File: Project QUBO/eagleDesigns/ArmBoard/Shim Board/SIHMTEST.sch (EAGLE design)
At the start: 10 parts, among them U1 BME280

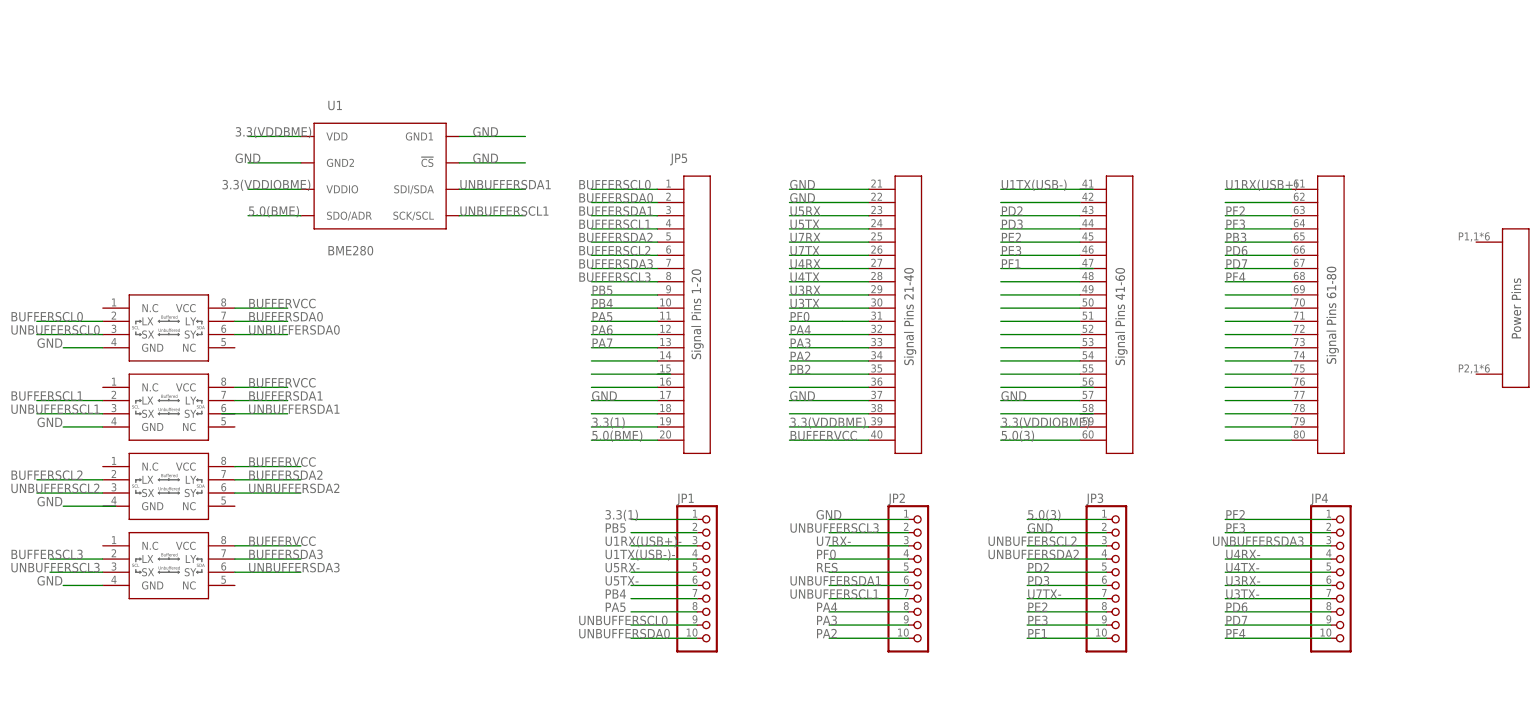
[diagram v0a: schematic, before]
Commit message: 
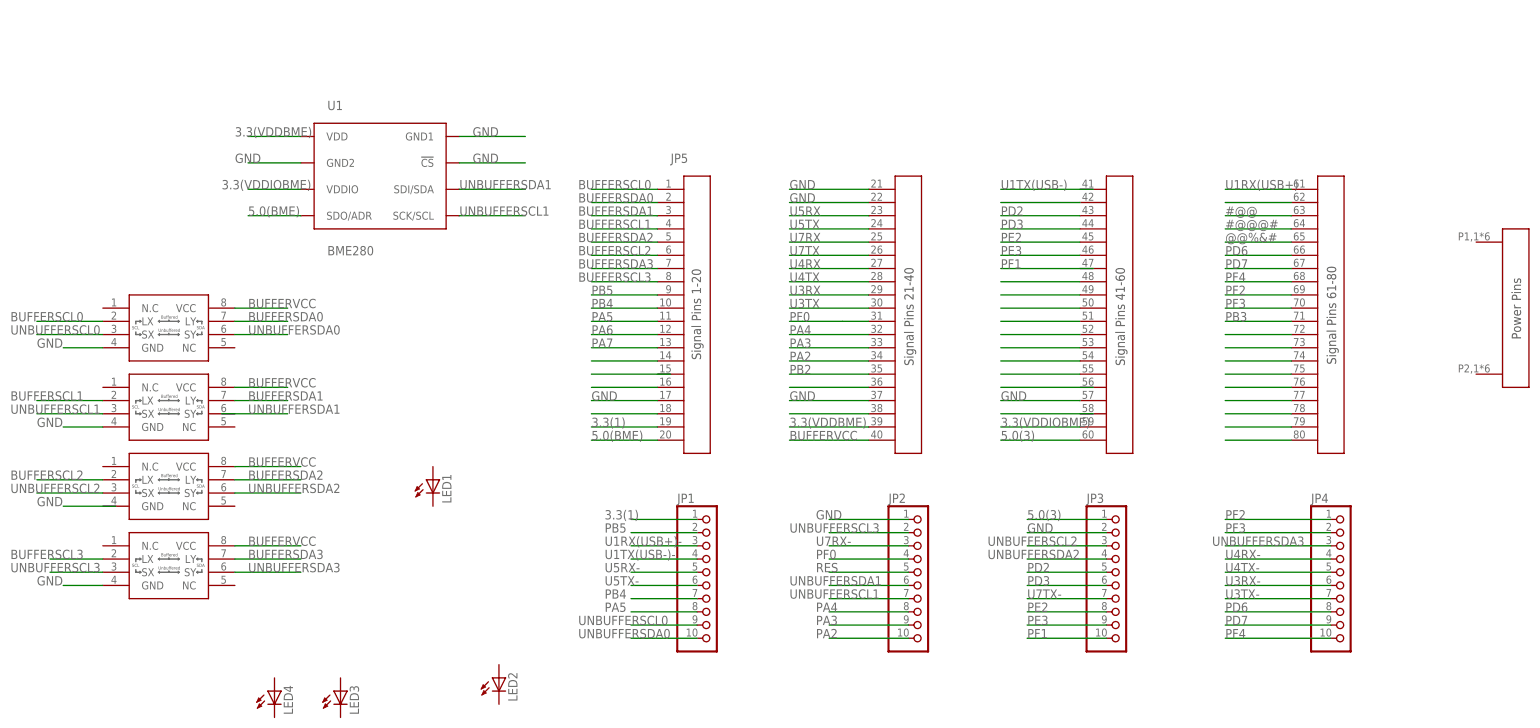
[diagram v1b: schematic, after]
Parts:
- added LED1, LED2, LED3, LED4: (no value), led:LEDCHIPLED_0805
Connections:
- removed net N$38: JP5.P$69
- removed net N$39: JP5.P$70
- removed net N$40: JP5.P$71
- new net #@@: JP5.P$63
- new net #@@@#: JP5.P$64
- new net @@%&#: JP5.P$65
- net PB3: now also JP5.P$71; no longer JP5.P$65
- net PF2: now also JP5.P$69; no longer JP5.P$63
- net PF3: now also JP5.P$70; no longer JP5.P$64

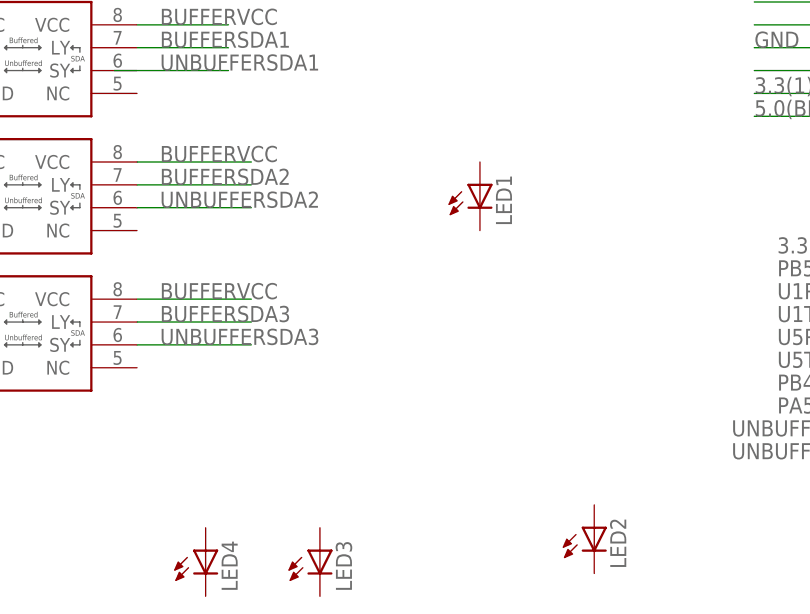
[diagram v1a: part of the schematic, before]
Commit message: 
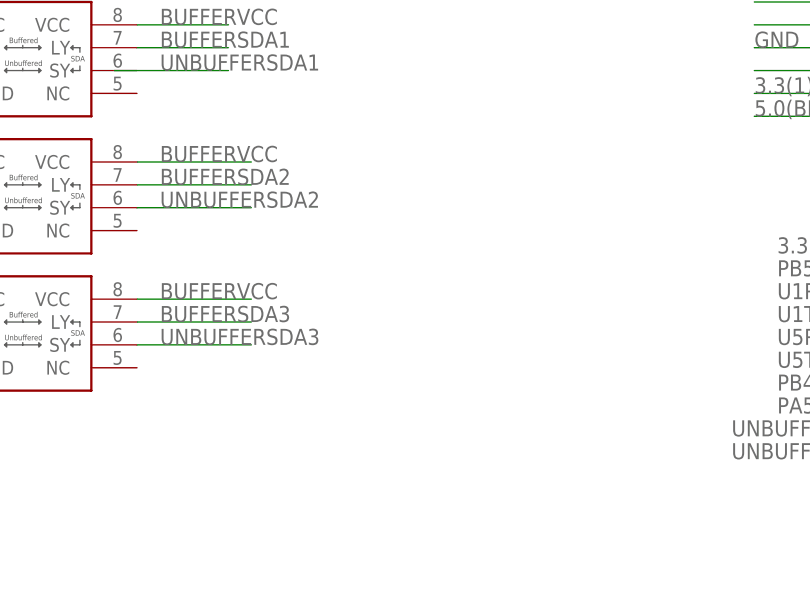
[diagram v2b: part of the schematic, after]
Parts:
- removed LED1, LED2, LED3, LED4: (no value), led:LEDCHIPLED_0805
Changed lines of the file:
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@@
 <part name="U$3" library="NXP" deviceset="P82B715" device=""/>
 <part name="U$4" library="NXP" deviceset="P82B715" device=""/>
-<part name="LED1" library="led" deviceset="LED" device="CHIPLED_0805"/>
-<part name="LED2" library="led" deviceset="LED" device="CHIPLED_0805"/>
-<part name="LED3" library="led" deviceset="LED" device="CHIPLED_0805"/>
-<part name="LED4" library="led" deviceset="LED" device="CHIPLED_0805"/>
 </parts>
 <sheets>
@@
 <instance part="U$3" gate="G$1" x="-86.36" y="93.98"/>
 <instance part="U$4" gate="G$1" x="-86.36" y="78.74"/>
-<instance part="LED1" gate="G$1" x="-35.56" y="96.52"/>
-<instance part="LED2" gate="G$1" x="-22.86" y="58.42"/>
-<instance part="LED3" gate="G$1" x="-53.34" y="55.88"/>
-<instance part="LED4" gate="G$1" x="-66.04" y="55.88"/>
 </instances>
 <busses>

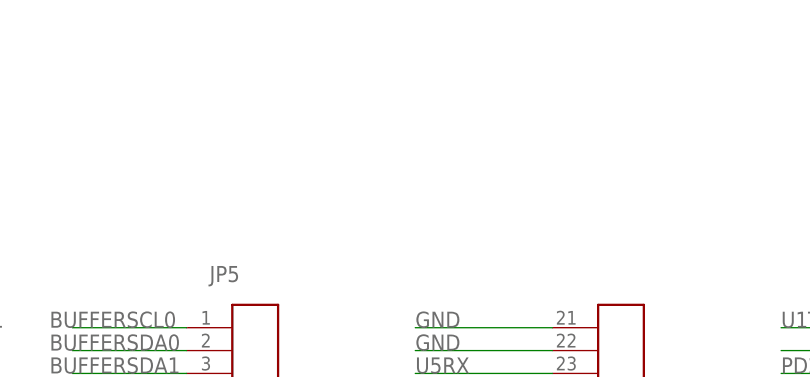
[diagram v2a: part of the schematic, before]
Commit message: 
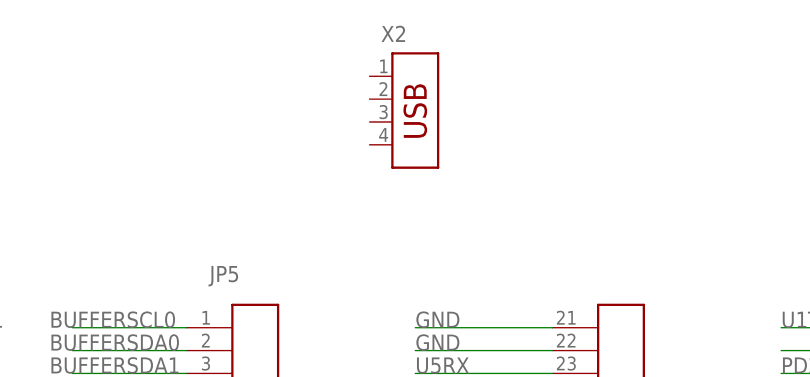
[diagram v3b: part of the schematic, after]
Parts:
- added X2: (no value), con-amp:USB-787616
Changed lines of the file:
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@@
 <part name="U$3" library="NXP" deviceset="P82B715" device=""/>
 <part name="U$4" library="NXP" deviceset="P82B715" device=""/>
+<part name="X2" library="con-amp" deviceset="USB-787616" device=""/>
 </parts>
 <sheets>
@@
 <instance part="U$3" gate="G$1" x="-86.36" y="93.98"/>
 <instance part="U$4" gate="G$1" x="-86.36" y="78.74"/>
+<instance part="X2" gate="G$1" x="33.02" y="175.26"/>
 </instances>
 <busses>

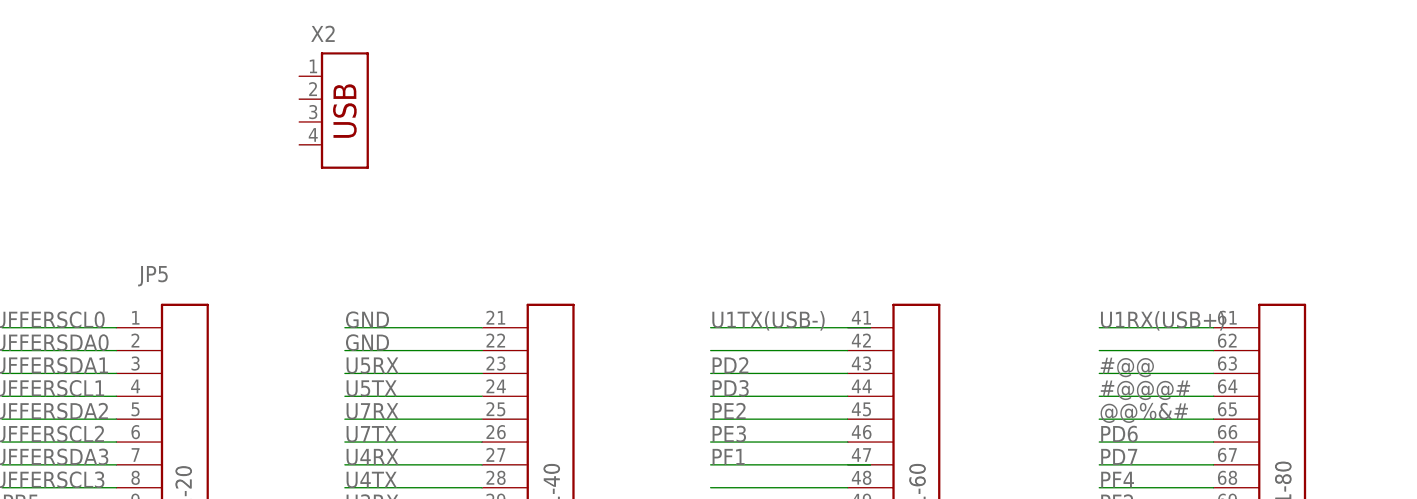
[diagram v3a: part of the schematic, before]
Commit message: 
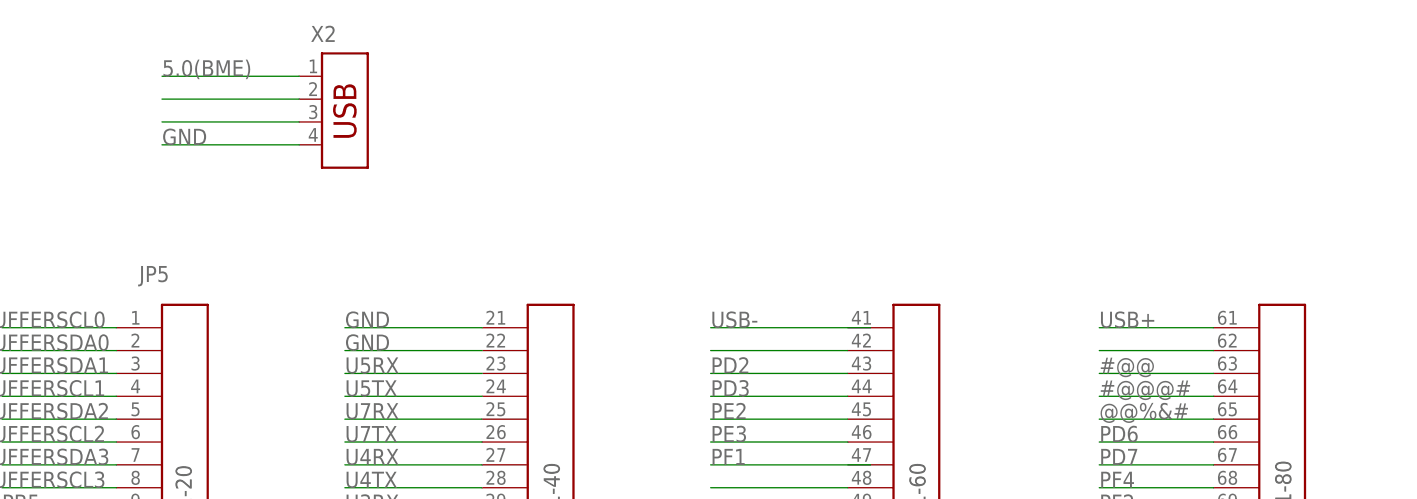
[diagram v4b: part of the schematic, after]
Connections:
- net U1RX(USB+) renamed USB+
- new net N$4: X2.2
- new net N$5: X2.3
- net 5.0(BME): now also X2.1
- net GND: now also X2.4
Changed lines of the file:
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@@
 </segment>
 </net>
-<net name="U1RX(USB+)" class="0">
+<net name="USB+" class="0">
 <segment>
 <pinref part="JP5" gate="G$1" pin="P$61"/>
@@
 </segment>
 </net>
-<net name="U1TX(USB-)" class="0">
+<net name="USB-" class="0">
 <segment>
 <wire x1="91.44" y1="152.4" x2="73.66" y2="152.4" width="0.1524" layer="91"/>
@@
 <wire x1="-60.96" y1="147.32" x2="-71.12" y2="147.32" width="0.1524" layer="91"/>
 <label x="-71.12" y="147.32" size="1.778" layer="95"/>
+</segment>
+<segment>
+<pinref part="X2" gate="G$1" pin="1"/>
+<wire x1="27.94" y1="180.34" x2="12.7" y2="180.34" width="0.1524" layer="91"/>
+<label x="12.7" y="180.34" size="1.778" layer="95"/>
 </segment>
 </net>
@@
 <label x="33.02" y="149.86" size="1.778" layer="95"/>
 </segment>
+<segment>
+<pinref part="X2" gate="G$1" pin="4"/>
+<wire x1="27.94" y1="172.72" x2="12.7" y2="172.72" width="0.1524" layer="91"/>
+<label x="12.7" y="172.72" size="1.778" layer="95"/>
+</segment>
 </net>
 <net name="UNBUFFERSCL1" class="0">
@@
 </segment>
 </net>
+<net name="N$4" class="0">
+<segment>
+<pinref part="X2" gate="G$1" pin="2"/>
+<wire x1="27.94" y1="177.8" x2="12.7" y2="177.8" width="0.1524" layer="91"/>
+</segment>
+</net>
+<net name="N$5" class="0">
+<segment>
+<pinref part="X2" gate="G$1" pin="3"/>
+<wire x1="27.94" y1="175.26" x2="12.7" y2="175.26" width="0.1524" layer="91"/>
+</segment>
+</net>

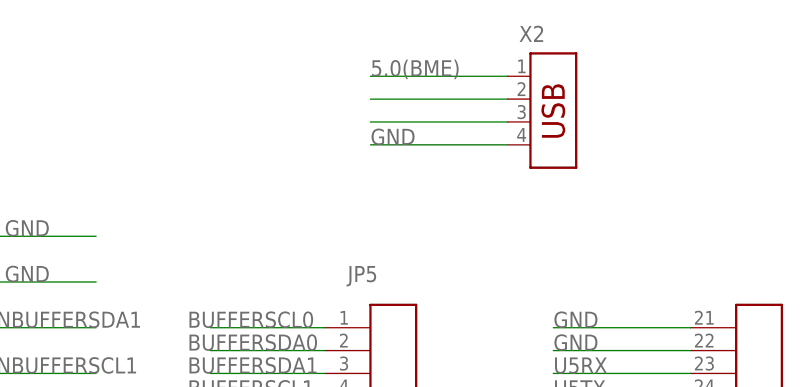
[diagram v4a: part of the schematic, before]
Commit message: 
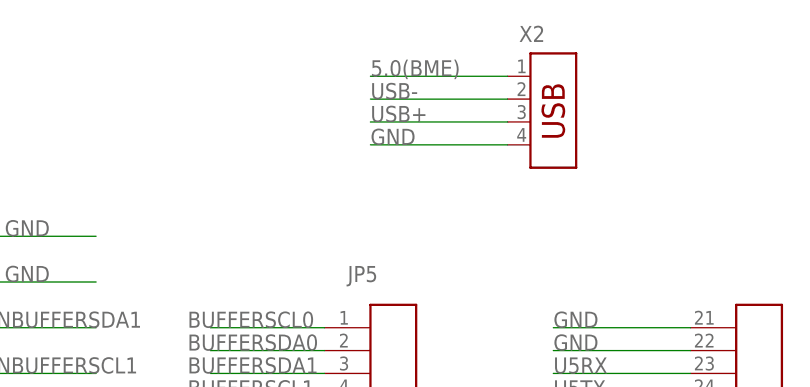
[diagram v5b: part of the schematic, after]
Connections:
- net N$4 renamed USB-
- removed net N$5: X2.3
- net USB+: now also X2.3
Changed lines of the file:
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@@
 <label x="116.84" y="152.4" size="1.778" layer="95"/>
+</segment>
+<segment>
+<pinref part="X2" gate="G$1" pin="3"/>
+<wire x1="27.94" y1="175.26" x2="12.7" y2="175.26" width="0.1524" layer="91"/>
+<label x="12.7" y="175.26" size="1.778" layer="95"/>
 </segment>
 </net>
@@
 <wire x1="91.44" y1="152.4" x2="73.66" y2="152.4" width="0.1524" layer="91"/>
 <label x="73.66" y="152.4" size="1.778" layer="95"/>
+</segment>
+<segment>
+<pinref part="X2" gate="G$1" pin="2"/>
+<wire x1="27.94" y1="177.8" x2="12.7" y2="177.8" width="0.1524" layer="91"/>
+<label x="12.7" y="177.8" size="1.778" layer="95"/>
 </segment>
 </net>
@@
 </segment>
 </net>
-<net name="N$4" class="0">
-<segment>
-<pinref part="X2" gate="G$1" pin="2"/>
-<wire x1="27.94" y1="177.8" x2="12.7" y2="177.8" width="0.1524" layer="91"/>
-</segment>
-</net>
-<net name="N$5" class="0">
-<segment>
-<pinref part="X2" gate="G$1" pin="3"/>
-<wire x1="27.94" y1="175.26" x2="12.7" y2="175.26" width="0.1524" layer="91"/>
-</segment>
-</net>

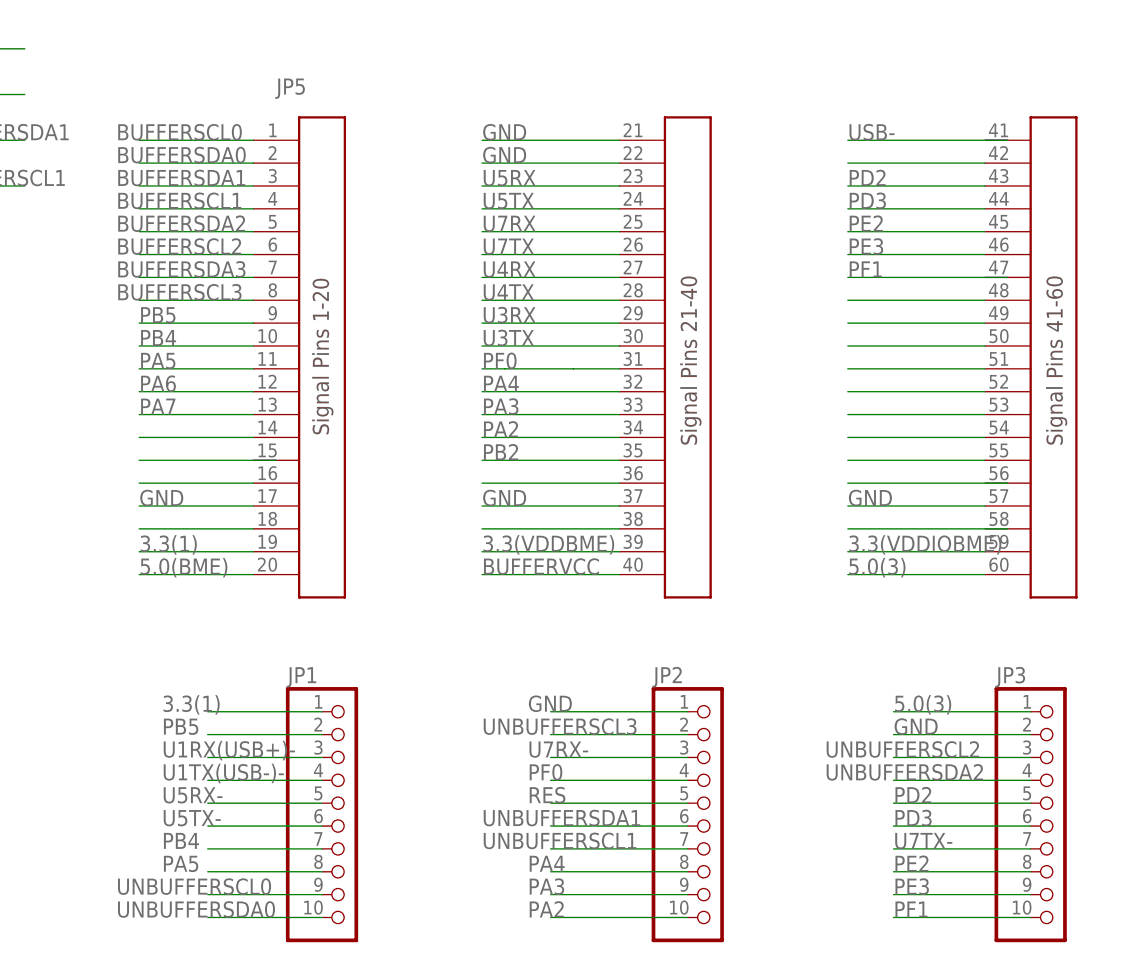
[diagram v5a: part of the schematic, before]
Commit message: 
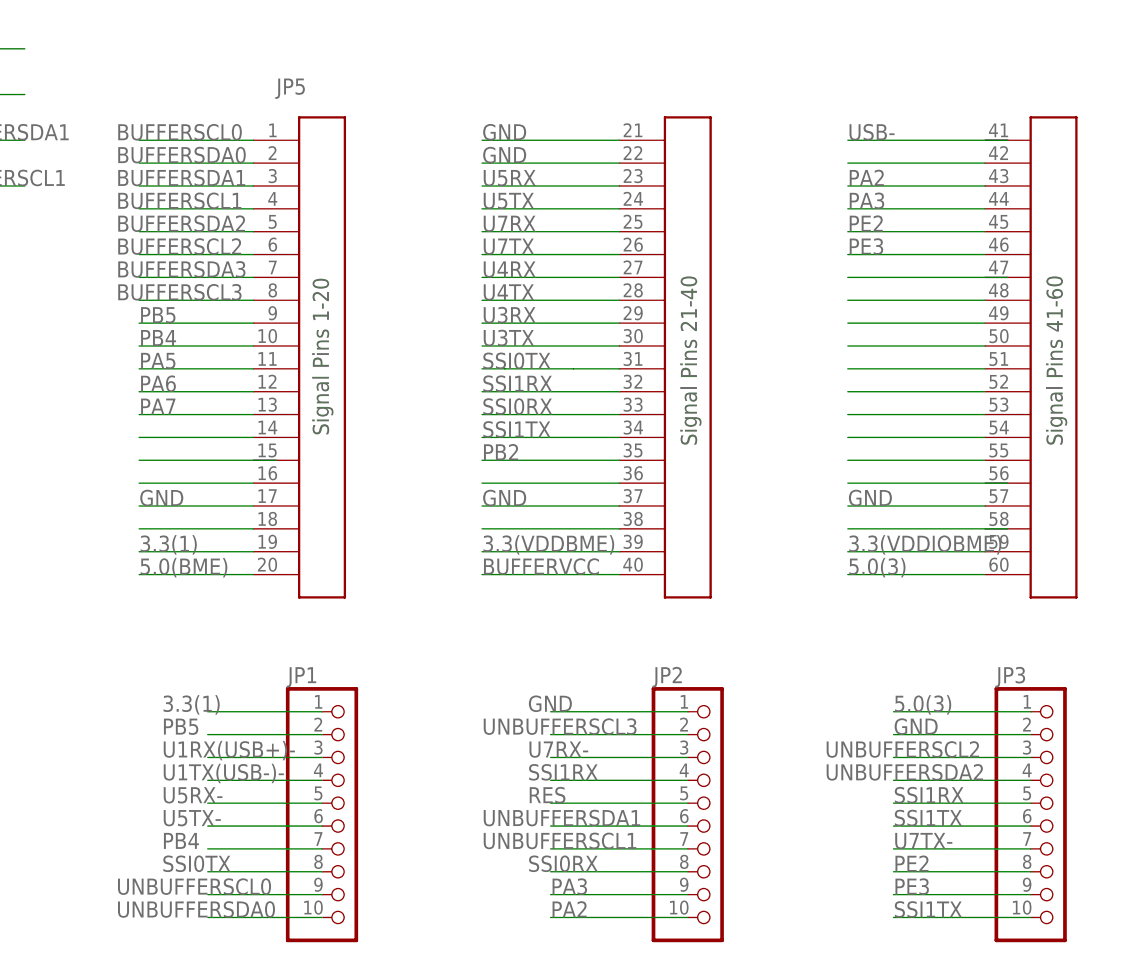
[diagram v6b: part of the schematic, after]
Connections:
- removed net PA4: JP2.8, JP5.P$32
- removed net PD2: JP3.5, JP5.P$43
- removed net PD3: JP3.6, JP5.P$44
- removed net PF0: JP2.4, JP5.P$31
- removed net PF1: JP3.10
- new net SSI0RX: JP2.8, JP5.P$33
- new net SSI0TX: JP1.8, JP5.P$31
- new net SSI1RX: JP2.4, JP3.5, JP5.P$32
- new net SSI1TX: JP3.10, JP3.6, JP5.P$34
- net PA2: now also JP5.P$43; no longer JP5.P$34
- net PA3: now also JP5.P$44; no longer JP5.P$33
- net PA5: no longer JP1.8
